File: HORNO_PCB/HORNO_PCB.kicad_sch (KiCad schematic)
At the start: 105 parts, among them J0_1 Terminales de tornillo espaci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, J0_10 Terminales de tornillo espaci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, J0_13 Terminales de tornillo espaci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, J0_14 Terminales de tornillo espaci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, J0_18 Terminales de tornillo espaci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, J0_3 Terminales de tornillo espaci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, J0_4 Terminales de tornillo espaci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, J0_5 Terminales de tornillo espaci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, J0_6 Terminales de tornillo espaci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, J0_7 Terminales de tornillo espaci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, J0_8 Terminales de tornillo espaci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, J0_9 Terminales de tornillo espaci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, J1 switch, J10 switch, J11 switch, J12 switch, J13 switch, J14 switch, J15 switch, J16 switch, J17 switch, J18 switch, J19 switch, J2 switch, J20 switch, J21 switch, J22 switch, J23 switch, J24 Screw_Terminal_01x20, J25 Screw_Terminal_01x20, J26 Screw_Terminal_01x20, J27 Screw_Terminal_01x20, J3 switch, J4 switch, J5 switch, J6 switch, J7 24VDC, J8 switch, J9 switch, K1 Relay 1, K2 Relay 2, K6 Relay 4, K7 Relay 3, K8 Relay 2, K9 Relay 1, Q1 2N2222, Q2 2N2222, Q6 IRG4PF50W, Q7 IRG4PF50W, U1 TLP521-1, U10 LM741, U15 TLP250, U17 LM741, U18 LM741, U19 TLP250, U2 TLP521-1, U25 UDN2981A, U3 TLP521-1, U4 TLP521-1, U9 LM741

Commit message: Actualización de PCB
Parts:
- added J28, J29: switch, TerminalBlock_MetzConnect:TerminalBlock_MetzConnect_360271_1x01_Horizontal_ScrewM3.0_Boxed, symbol Connector:Screw_Terminal_01x01
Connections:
- net at D10.2 (A), D11.2 (A), D12.2 (A)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: now also J29.1 (Pin_1); no longer R12.1
- new net: J28.1 (Pin_1), R12.1
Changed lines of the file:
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@@
 	)
 	(junction
-		(at 133.35 353.06)
-		(diameter 0)
-		(color 0 0 0 0)
-	)
-	(junction
 		(at 568.96 273.05)
 		(diameter 0)
@@
 	)
 	(junction
+		(at 105.41 353.06)
+		(diameter 0)
+		(color 0 0 0 0)
+	)
+	(junction
 		(at 839.47 570.23)
 		(diameter 0)
@@
 	)
 	(junction
+		(at 119.38 353.06)
+		(diameter 0)
+		(color 0 0 0 0)
+	)
+	(junction
 		(at 212.09 314.96)
 		(diameter 0)
@@
 	)
 	(junction
-		(at 119.38 353.06)
-		(diameter 0)
-		(color 0 0 0 0)
-	)
-	(junction
 		(at 1112.52 373.38)
 		(diameter 0)
@@
 	)
 	(junction
-		(at 105.41 353.06)
+		(at 683.26 462.28)
 		(diameter 0)
 		(color 0 0 0 0)
 	)
 	(junction
-		(at 683.26 462.28)
+		(at 918.21 482.6)
 		(diameter 0)
 		(color 0 0 0 0)
 	)
 	(junction
-		(at 918.21 482.6)
+		(at 186.69 337.82)
 		(diameter 0)
 		(color 0 0 0 0)
 	)
 	(junction
-		(at 186.69 337.82)
+		(at 133.35 353.06)
 		(diameter 0)
 		(color 0 0 0 0)
@@
 	(wire
 		(pts
-			(xy 105.41 353.06) (xy 119.38 353.06)
-		)
-		(stroke
-			(width 0)
-			(type default)
-			(color 255 11 0 1)
-		)
-	)
-	(wire
-		(pts
 			(xy 278.13 200.66) (xy 278.13 289.56)
 		)
@@
 	(wire
 		(pts
-			(xy 119.38 353.06) (xy 133.35 353.06)
-		)
-		(stroke
-			(width 0)
-			(type default)
-			(color 255 11 0 1)
-		)
-	)
-	(wire
-		(pts
 			(xy 466.09 147.32) (xy 513.08 147.32)
 		)
@@
 	(wire
 		(pts
+			(xy 133.35 351.79) (xy 133.35 353.06)
+		)
+		(stroke
+			(width 0)
+			(type default)
+			(color 255 11 0 1)
+		)
+	)
+	(wire
+		(pts
 			(xy 133.35 772.16) (xy 632.46 772.16)
 		)
@@
 	(wire
 		(pts
+			(xy 93.98 353.06) (xy 105.41 353.06)
+		)
+		(stroke
+			(width 0)
+			(type default)
+			(color 255 11 0 1)
+		)
+	)
+	(wire
+		(pts
 			(xy 431.8 554.99) (xy 431.8 541.02)
 		)
@@
 	(wire
 		(pts
-			(xy 93.98 353.06) (xy 105.41 353.06)
-		)
-		(stroke
-			(width 0)
-			(type default)
-			(color 255 11 0 1)
-		)
-	)
-	(wire
-		(pts
-			(xy 133.35 332.74) (xy 133.35 353.06)
-		)
-		(stroke
-			(width 0)
-			(type default)
-			(color 255 11 0 1)
-		)
-	)
-	(wire
-		(pts
 			(xy 872.49 549.91) (xy 872.49 582.93)
 		)
@@
 	(wire
 		(pts
-			(xy 133.35 353.06) (xy 133.35 772.16)
-		)
-		(stroke
-			(width 0)
-			(type default)
-			(color 255 11 0 1)
-		)
-	)
-	(wire
-		(pts
 			(xy 436.88 629.92) (xy 436.88 562.61)
 		)
@@
 	(wire
 		(pts
+			(xy 119.38 353.06) (xy 133.35 353.06)
+		)
+		(stroke
+			(width 0)
+			(type default)
+			(color 255 11 0 1)
+		)
+	)
+	(wire
+		(pts
 			(xy 500.38 622.3) (xy 516.89 622.3)
 		)
@@
 	(wire
 		(pts
+			(xy 105.41 353.06) (xy 119.38 353.06)
+		)
+		(stroke
+			(width 0)
+			(type default)
+			(color 255 11 0 1)
+		)
+	)
+	(wire
+		(pts
 			(xy 383.54 567.69) (xy 387.35 567.69)
 		)
@@
 	(wire
 		(pts
+			(xy 133.35 353.06) (xy 133.35 772.16)
+		)
+		(stroke
+			(width 0)
+			(type default)
+			(color 255 11 0 1)
+		)
+	)
+	(wire
+		(pts
 			(xy 858.52 549.91) (xy 872.49 549.91)
 		)
@@
 	(symbol
 		(lib_id "Connector:Screw_Terminal_01x01")
+		(at 133.35 346.71 90)
+		(unit 1)
+		(exclude_from_sim no)
+		(in_bom yes)
+		(on_board yes)
+		(dnp no)
+		(fields_autoplaced yes)
+		(property "Reference" "J29"
+			(at 135.89 346.7099 90)
+			(effects
+				(font
+					(size 1.27 1.27)
+				)
+				(justify right)
+			)
+		)
+		(property "Value" "switch"
+			(at 130.81 345.4401 90)
+			(effects
+				(font
+					(size 1.27 1.27)
+				)
+				(justify left)
+				(hide yes)
+			)
+		)
+		(property "Footprint" "TerminalBlock_MetzConnect:TerminalBlock_MetzConnect_360271_1x01_Horizontal_ScrewM3.0_Boxed"
+			(at 133.35 346.71 0)
+			(effects
+				(font
+					(size 1.27 1.27)
+				)
+				(hide yes)
+			)
+		)
+		(property "Datasheet" "~"
+			(at 133.35 346.71 0)
+			(effects
+				(font
+					(size 1.27 1.27)
+				)
+				(hide yes)
+			)
+		)
+		(property "Description" "Generic screw terminal, single row, 01x01, script generated (kicad-library-utils/schlib/autogen/connector/)"
+			(at 133.35 346.71 0)
+			(effects
+				(font
+					(size 1.27 1.27)
+				)
+				(hide yes)
+			)
+		)
+		(pin "1"
+		)
+		(instances
+			(project "HORNO_PCB"
+				(path "/70384b34-09dd-4fe3-975b-9645e85de3d4"
+					(reference "J29")
+					(unit 1)
+				)
+			)
+		)
+	)
+	(symbol
+		(lib_id "Connector:Screw_Terminal_01x01")
 		(at 684.53 662.94 90)
 		(unit 1)
@@
 					(unit 1)
 				)
+			)
+		)
+	)
+	(symbol
+		(lib_id "Connector:Screw_Terminal_01x01")
+		(at 133.35 337.82 270)
+		(unit 1)
+		(exclude_from_sim no)
+		(in_bom yes)
+		(on_board yes)
+		(dnp no)
+		(fields_autoplaced yes)
+		(property "Reference" "J28"
+			(at 135.89 336.5499 90)
+			(effects
+				(font
+					(size 1.27 1.27)
+				)
+				(justify left)
+			)
+		)
+		(property "Value" "switch"
+			(at 135.89 339.0899 90)
+			(effects
+				(font
+					(size 1.27 1.27)
+				)
+				(justify left)
+				(hide yes)
+			)
+		)
+		(property "Footprint" "TerminalBlock_MetzConnect:TerminalBlock_MetzConnect_360271_1x01_Horizontal_ScrewM3.0_Boxed"
+			(at 133.35 337.82 0)
+			(effects
+				(font
+					(size 1.27 1.27)
+				)
+				(hide yes)
+			)
+		)
+		(property "Datasheet" "~"
+			(at 133.35 337.82 0)
+			(effects
+				(font
+					(size 1.27 1.27)
+				)
+				(hide yes)
+			)
+		)
+		(property "Description" "Generic screw terminal, single row, 01x01, script generated (kicad-library-utils/schlib/autogen/connector/)"
+			(at 133.35 337.82 0)
+			(effects
+				(font
+					(size 1.27 1.27)
+				)
+				(hide yes)
+			)
+		)
+		(pin "1"
+		)
+		(instances
+			(project "HORNO_PCB"
+				(path "/70384b34-09dd-4fe3-975b-9645e85de3d4"
+					(reference "J28")
+					(unit 1)
+				)

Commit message: Actualizacion de PCB
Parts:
- removed J1, J2, J28, J29, J3, J4, J5, J6: switch, TerminalBlock_MetzConnect:TerminalBlock_MetzConnect_360271_1x01_Horizontal_ScrewM3.0_Boxed, symbol Connector:Screw_Terminal_01x01
- added J0_11, J0_12, J0_15, J0_2: Terminales de tornillo espaciados en 5mm, TerminalBlock_Phoenix:TerminalBlock_Phoenix_PT-1,5-3-5.0-H_1x03_P5.00mm_Horizontal, symbol Connector:Screw_Terminal_01x03
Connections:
- net at R7.1: now also J0_11.1 (Pin_1)
- net at D10.2 (A), D11.2 (A), D12.2 (A)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: now also J0_11.3 (Pin_3), J0_12.3 (Pin_3), J0_15.3 (Pin_3), J0_2.3 (Pin_3)
- net at R8.1: now also J0_12.1 (Pin_1)
- net at R28.1: now also J0_2.1 (Pin_1)
- net at R12.1: now also J0_15.1 (Pin_1)

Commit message: Actualizacion de PCB
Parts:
- added J1: switch, TerminalBlock_MetzConnect:TerminalBlock_MetzConnect_360271_1x01_Horizontal_ScrewM3.0_Boxed, symbol Connector:Screw_Terminal_01x01
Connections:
- net at J11.1 (Pin_1), J21.1 (Pin_1), J24.2 (Pin_2)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: no longer J0_1.1 (Pin_1), J0_1.2 (Pin_2), J0_1.3 (Pin_3)
- new net: J0_1.1 (Pin_1), J0_1.2 (Pin_2), J0_1.3 (Pin_3), J1.1 (Pin_1)
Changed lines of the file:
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@@
 	)
 	(junction
-		(at 492.76 149.86)
-		(diameter 0)
-		(color 0 0 0 0)
-	)
-	(junction
 		(at 622.3 675.64)
 		(diameter 0)
@@
 	)
 	(junction
-		(at 487.68 149.86)
-		(diameter 0)
-		(color 0 0 0 0)
-	)
-	(junction
 		(at 977.9 336.55)
 		(diameter 0)
@@
 	)
 	(junction
-		(at 490.22 149.86)
+		(at 490.22 120.65)
 		(diameter 0)
 		(color 0 0 0 0)
@@
 	(wire
 		(pts
+			(xy 490.22 111.76) (xy 490.22 120.65)
+		)
+		(stroke
+			(width 0)
+			(type default)
+			(color 255 6 0 1)
+		)
+	)
+	(wire
+		(pts
 			(xy 825.5 120.65) (xy 652.78 120.65)
 		)
@@
 	(wire
 		(pts
-			(xy 490.22 149.86) (xy 492.76 149.86)
+			(xy 191.77 314.96) (xy 195.58 314.96)
 		)
 		(stroke
 			(width 0)
 			(type default)
-			(color 255 6 0 1)
 		)
 	)
 	(wire
 		(pts
-			(xy 191.77 314.96) (xy 195.58 314.96)
+			(xy 763.27 462.28) (xy 763.27 525.78)
 		)
 		(stroke
@@
 	(wire
 		(pts
-			(xy 763.27 462.28) (xy 763.27 525.78)
+			(xy 464.82 629.92) (xy 478.79 629.92)
 		)
 		(stroke
@@
 	(wire
 		(pts
-			(xy 464.82 629.92) (xy 478.79 629.92)
+			(xy 417.83 622.3) (xy 433.07 622.3)
 		)
 		(stroke
@@
 	(wire
 		(pts
-			(xy 417.83 622.3) (xy 433.07 622.3)
+			(xy 887.73 486.41) (xy 887.73 603.25)
 		)
 		(stroke
 			(width 0)
 			(type default)
+			(color 0 0 0 1)
 		)
 	)
 	(wire
 		(pts
-			(xy 887.73 486.41) (xy 887.73 603.25)
+			(xy 528.32 170.18) (xy 528.32 124.46)
 		)
 		(stroke
 			(width 0)
 			(type default)
-			(color 0 0 0 1)
 		)
 	)
 	(wire
 		(pts
-			(xy 528.32 170.18) (xy 528.32 124.46)
+			(xy 492.76 111.76) (xy 492.76 120.65)
 		)
 		(stroke
 			(width 0)
 			(type default)
+			(color 255 6 0 1)
 		)
 	)
@@
 	(wire
 		(pts
-			(xy 490.22 111.76) (xy 490.22 149.86)
-		)
-		(stroke
-			(width 0)
-			(type default)
-			(color 255 6 0 1)
-		)
-	)
-	(wire
-		(pts
 			(xy 391.16 629.92) (xy 391.16 562.61)
 		)
@@
 	(wire
 		(pts
+			(xy 490.22 120.65) (xy 490.22 127)
+		)
+		(stroke
+			(width 0)
+			(type default)
+			(color 255 6 0 1)
+		)
+	)
+	(wire
+		(pts
 			(xy 575.31 293.37) (xy 575.31 320.04)
 		)
@@
 	(wire
 		(pts
+			(xy 492.76 120.65) (xy 490.22 120.65)
+		)
+		(stroke
+			(width 0)
+			(type default)
+			(color 255 6 0 1)
+		)
+	)
+	(wire
+		(pts
 			(xy 674.37 477.52) (xy 665.48 477.52)
 		)
@@
 	(wire
 		(pts
-			(xy 417.83 149.86) (xy 487.68 149.86)
-		)
-		(stroke
-			(width 0)
-			(type default)
-			(color 255 6 0 1)
-		)
-	)
-	(wire
-		(pts
 			(xy 822.96 666.75) (xy 822.96 683.26)
 		)
@@
 	(wire
 		(pts
-			(xy 487.68 111.76) (xy 487.68 149.86)
-		)
-		(stroke
-			(width 0)
-			(type default)
-			(color 255 6 0 1)
-		)
-	)
-	(wire
-		(pts
 			(xy 481.33 463.55) (xy 496.57 463.55)
 		)
@@
 	(wire
 		(pts
-			(xy 492.76 149.86) (xy 563.88 149.86)
+			(xy 417.83 149.86) (xy 563.88 149.86)
 		)
 		(stroke
@@
 	(wire
 		(pts
+			(xy 487.68 111.76) (xy 487.68 120.65)
+		)
+		(stroke
+			(width 0)
+			(type default)
+			(color 255 6 0 1)
+		)
+	)
+	(wire
+		(pts
 			(xy 593.09 116.84) (xy 588.01 116.84)
 		)
@@
 	(wire
 		(pts
-			(xy 492.76 111.76) (xy 492.76 149.86)
-		)
-		(stroke
-			(width 0)
-			(type default)
-			(color 255 6 0 1)
-		)
-	)
-	(wire
-		(pts
 			(xy 171.45 284.48) (xy 163.83 284.48)
 		)
@@
 	(wire
 		(pts
-			(xy 695.96 110.49) (xy 652.78 110.49)
+			(xy 487.68 120.65) (xy 490.22 120.65)
 		)
 		(stroke
 			(width 0)
 			(type default)
+			(color 255 6 0 1)
 		)
 	)
 	(wire
 		(pts
-			(xy 669.29 441.96) (xy 669.29 440.69)
+			(xy 695.96 110.49) (xy 652.78 110.49)
 		)
 		(stroke
 			(width 0)
 			(type default)
-			(color 0 0 0 1)
 		)
 	)
 	(wire
 		(pts
-			(xy 789.94 683.26) (xy 789.94 626.11)
+			(xy 669.29 441.96) (xy 669.29 440.69)
 		)
 		(stroke
 			(width 0)
 			(type default)
-			(color 255 6 0 1)
+			(color 0 0 0 1)
 		)
 	)
 	(wire
 		(pts
-			(xy 505.46 629.92) (xy 520.7 629.92)
+			(xy 789.94 683.26) (xy 789.94 626.11)
 		)
 		(stroke
 			(width 0)
 			(type default)
+			(color 255 6 0 1)
 		)
 	)
 	(wire
 		(pts
-			(xy 487.68 149.86) (xy 490.22 149.86)
+			(xy 505.46 629.92) (xy 520.7 629.92)
 		)
 		(stroke
 			(width 0)
 			(type default)
-			(color 255 6 0 1)
 		)
 	)
@@
 					(unit 1)
 				)
+			)
+		)
+	)
+	(symbol
+		(lib_id "Connector:Screw_Terminal_01x01")
+		(at 490.22 132.08 270)
+		(unit 1)
+		(exclude_from_sim no)
+		(in_bom yes)
+		(on_board yes)
+		(dnp no)
+		(fields_autoplaced yes)
+		(property "Reference" "J1"
+			(at 492.76 130.8099 90)
+			(effects
+				(font
+					(size 1.27 1.27)
+				)
+				(justify left)
+			)
+		)
+		(property "Value" "switch"
+			(at 492.76 133.3499 90)
+			(effects
+				(font
+					(size 1.27 1.27)
+				)
+				(justify left)
+				(hide yes)
+			)
+		)
+		(property "Footprint" "TerminalBlock_MetzConnect:TerminalBlock_MetzConnect_360271_1x01_Horizontal_ScrewM3.0_Boxed"
+			(at 490.22 132.08 0)
+			(effects
+				(font
+					(size 1.27 1.27)
+				)
+				(hide yes)
+			)
+		)
+		(property "Datasheet" "~"
+			(at 490.22 132.08 0)
+			(effects
+				(font
+					(size 1.27 1.27)
+				)
+				(hide yes)
+			)
+		)
+		(property "Description" "Generic screw terminal, single row, 01x01, script generated (kicad-library-utils/schlib/autogen/connector/)"
+			(at 490.22 132.08 0)
+			(effects
+				(font
+					(size 1.27 1.27)
+				)
+				(hide yes)
+			)
+		)
+		(pin "1"
+		)
+		(instances
+			(project "HORNO_PCB"
+				(path "/70384b34-09dd-4fe3-975b-9645e85de3d4"
+					(reference "J1")
+					(unit 1)
+				)

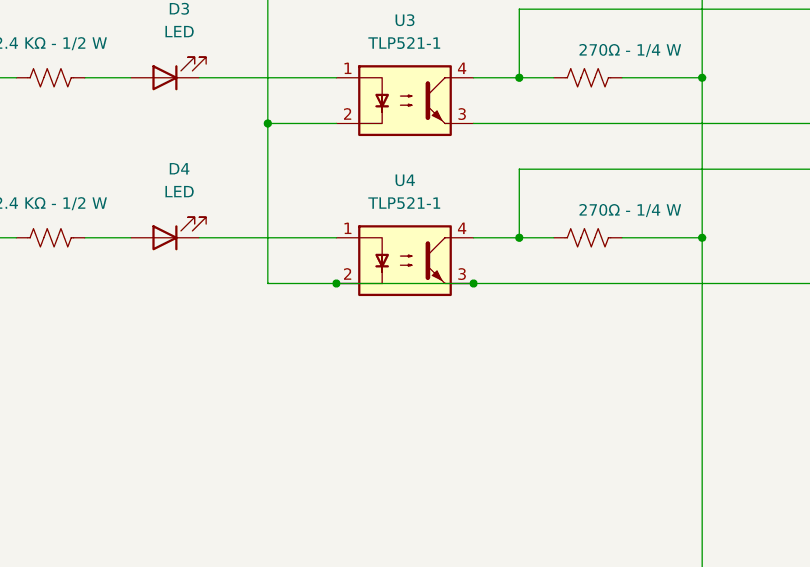
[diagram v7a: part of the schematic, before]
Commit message: Tamaño de PCB  y ruteo
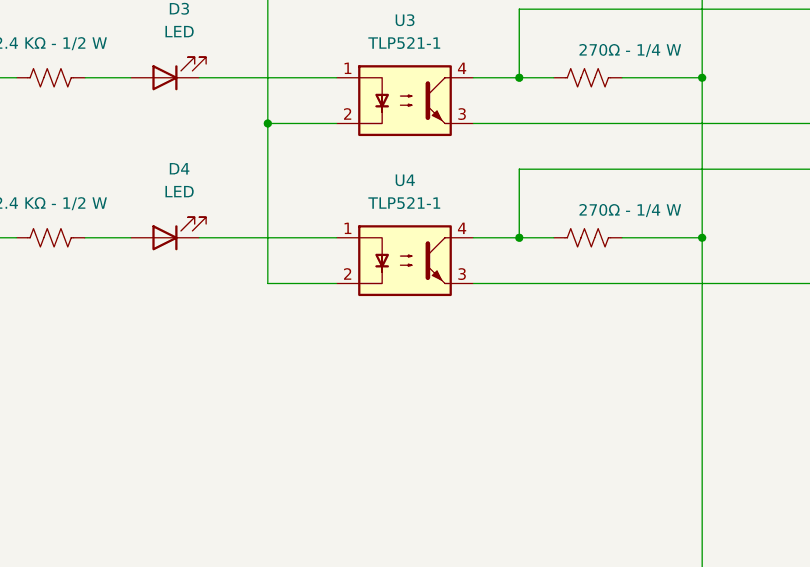
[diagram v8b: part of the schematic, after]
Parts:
- J0_1: value Terminales de tornillo espaciados en 5mm -> Alimentacion dispositivo serial
- J1: value switch -> +5V +24V
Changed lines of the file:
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@@
 	)
 	(junction
-		(at 171.45 337.82)
-		(diameter 0)
-		(color 0 0 0 0)
-	)
-	(junction
 		(at 683.26 462.28)
 		(diameter 0)
@@
 	)
 	(junction
-		(at 186.69 337.82)
-		(diameter 0)
-		(color 0 0 0 0)
-	)
-	(junction
 		(at 133.35 353.06)
 		(diameter 0)
@@
 	(wire
 		(pts
-			(xy 186.69 337.82) (xy 171.45 337.82)
-		)
-		(stroke
-			(width 0)
-			(type default)
-			(color 0 0 0 1)
-		)
-	)
-	(wire
-		(pts
 			(xy 466.09 111.76) (xy 466.09 147.32)
 		)
@@
 		)
 		(instances
-			(project ""
+			(project "HORNO_PCB"
 				(path "/70384b34-09dd-4fe3-975b-9645e85de3d4"
 					(reference "J7")
@@
 			)
 		)
-		(property "Value" "Terminales de tornillo espaciados en 5mm"
+		(property "Value" "Alimentacion dispositivo serial"
 			(at 488.9501 104.14 0)
 			(effects
@@
 			)
 		)
-		(property "Value" "switch"
+		(property "Value" "+5V     +24V"
 			(at 492.76 133.3499 90)
 			(effects
@@
 		)
 		(instances
-			(project ""
+			(project "HORNO_PCB"
 				(path "/70384b34-09dd-4fe3-975b-9645e85de3d4"
 					(reference "F1")
@@
 		)
 		(instances
-			(project ""
+			(project "HORNO_PCB"
 				(path "/70384b34-09dd-4fe3-975b-9645e85de3d4"
 					(reference "U25")
